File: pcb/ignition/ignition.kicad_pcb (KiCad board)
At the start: 4 copper layers, 100 x 100 mm, 142 parts, among them IC1 LTC4151, IC2 LTC4151, IC3 LTC4151, IC4 LTC4151, IC5 LTC4151, IC6 LTC4151, IC7 ADP3335, IC8 STM32F437VIT6, J1 PSU, J10 CH2, J11 CH4, J12 ARM, J13 UART1, J14 UART2, J15 CH1, J16 CH3, J17 CH5, J2 LED1, J3 PSU, J4 LED2, J5 5v In, J6 5v Out, J7 LED3, J8 LED4, J9 LED5, K1 16A SPST, K2 16A SPST, K3 16A SPST, K4 16A SPST, K5 16A SPST, K6 16A SPST, P1 SWD_TC, Q1 NFET, Q2 NFET, Q3 NFET, Q4 NFET, Q5 NFET, Q6 NFET, U1 MICROSD, X33 Hole, X34 Hole, X35 Hole, X36 Hole, Y1 26M

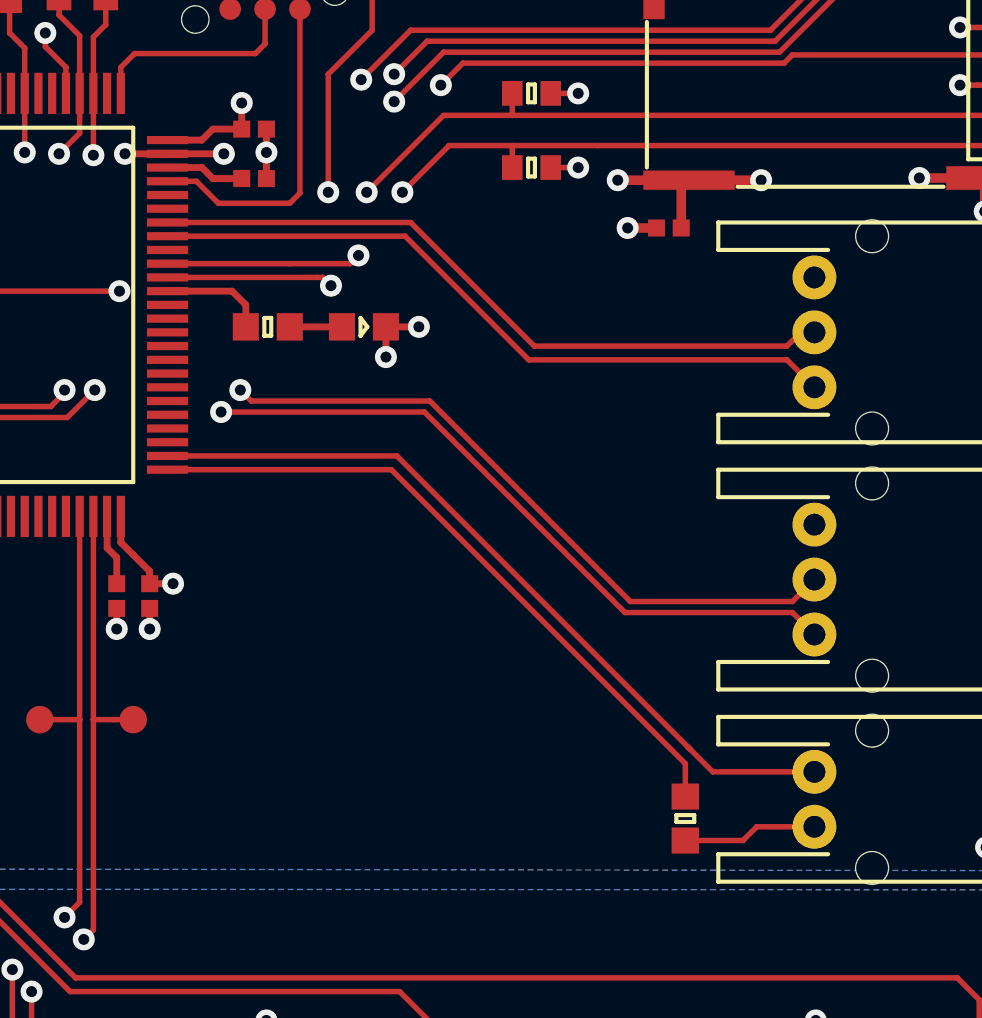
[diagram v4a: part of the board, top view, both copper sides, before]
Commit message: finalised schematic and pcb copper, adding silk
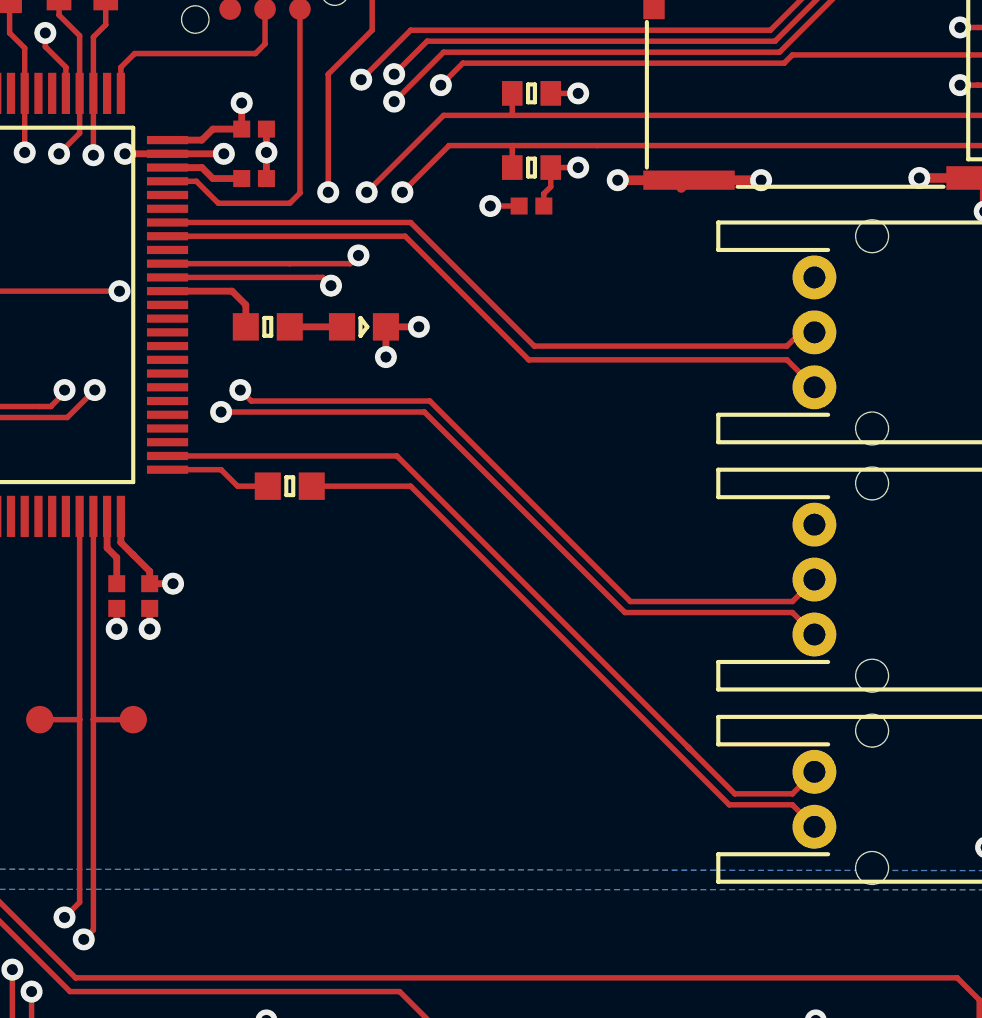
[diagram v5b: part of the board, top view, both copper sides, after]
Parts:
- moved R27 18.8 mm to (91.9, 45.6), turned to 180 degrees
- moved C19 5.06 mm to (100.7, 35.4), turned to 180 degrees
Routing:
- net /ARM_GRN: track 24.5 -> 3.90 mm
- net Net-(J12-Pad1): track 4.91 -> 23.4 mm
- net /ARM_RED: track 28.5 -> 29.1 mm
- net 3v3: track 227.3 -> 227.7 mm, vias 21 -> 20
- net GND: track 185.4 -> 185.0 mm, vias 84 -> 85
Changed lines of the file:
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@@
     (thickness 1.6)
     (drawings 4)
-    (tracks 1173)
+    (tracks 1177)
     (zones 0)
     (modules 142)
@@
   )
   (module agg:0402 (layer F.Cu)
-    (at 105.7 36.2)
-    (fp_text reference C19 (at -1.71 0 90) (layer F.Fab)
+    (at 100.7 35.4 180)
+    (fp_text reference C19 (at -1.71 0 270) (layer F.Fab)
       (effects (font (size 1 1) (thickness 0.15)))
     )
-    (fp_text value 100n (at 1.71 0 90) (layer F.Fab)
+    (fp_text value 100n (at 1.71 0 270) (layer F.Fab)
       (effects (font (size 1 1) (thickness 0.15)))
     )
@@
     (fp_line (start 0.5 -0.25) (end 0.5 0.25) (layer F.Fab) (width 0.01))
     (fp_line (start -0.5 -0.25) (end 0.5 -0.25) (layer F.Fab) (width 0.01))
-    (pad 2 smd rect (at 0.45 0) (size 0.62 0.62) (layers F.Cu F.Paste F.Mask)
+    (pad 2 smd rect (at 0.45 0 180) (size 0.62 0.62) (layers F.Cu F.Paste F.Mask)
       (net 2 GND))
-    (pad 1 smd rect (at -0.45 0) (size 0.62 0.62) (layers F.Cu F.Paste F.Mask)
+    (pad 1 smd rect (at -0.45 0 180) (size 0.62 0.62) (layers F.Cu F.Paste F.Mask)
       (net 15 3v3))
     (model ${KISYS3DMOD}/Resistors_SMD.3dshapes/R_0402.wrl
@@
   )
   (module agg:0603 (layer F.Cu)
-    (at 106.3 57.7 90)
-    (fp_text reference R27 (at -2.225 0 180) (layer F.Fab)
+    (at 91.9 45.6 180)
+    (fp_text reference R27 (at -2.225 0 270) (layer F.Fab)
       (effects (font (size 1 1) (thickness 0.15)))
     )
-    (fp_text value 100R (at 2.225 0 180) (layer F.Fab)
+    (fp_text value 100R (at 2.225 0 270) (layer F.Fab)
       (effects (font (size 1 1) (thickness 0.15)))
     )
@@
     (fp_line (start 0.8 -0.4) (end 0.8 0.4) (layer F.Fab) (width 0.01))
     (fp_line (start -0.8 -0.4) (end 0.8 -0.4) (layer F.Fab) (width 0.01))
-    (pad 2 smd rect (at 0.8 0 90) (size 0.95 1) (layers F.Cu F.Paste F.Mask)
+    (pad 2 smd rect (at 0.8 0 180) (size 0.95 1) (layers F.Cu F.Paste F.Mask)
       (net 76 /ARM_GRN))
-    (pad 1 smd rect (at -0.8 0 90) (size 0.95 1) (layers F.Cu F.Paste F.Mask)
+    (pad 1 smd rect (at -0.8 0 180) (size 0.95 1) (layers F.Cu F.Paste F.Mask)
       (net 122 "Net-(J12-Pad1)"))
     (model ${KISYS3DMOD}/Resistors_SMD.3dshapes/R_0603.wrl
@@
   (segment (start 117.2 35.16) (end 117.2 35.6) (width 0.35) (layer F.Cu) (net 2))
   (segment (start 106.15 34.745) (end 106.435 34.46) (width 0.35) (layer F.Cu) (net 2))
-  (segment (start 106.15 36.2) (end 106.15 34.745) (width 0.35) (layer F.Cu) (net 2))
+  (segment (start 100.25 35.4) (end 99.2 35.4) (width 0.2) (layer F.Cu) (net 2))
+  (via (at 99.2 35.4) (size 0.8) (drill 0.4) (layers F.Cu B.Cu) (net 2))
   (segment (start 43 95.8) (end 48.1 95.8) (width 0.35) (layer F.Cu) (net 3))
   (segment (start 48.1 95.8) (end 51 92.9) (width 0.35) (layer F.Cu) (net 3))
@@
   (via (at 116.3 28.9) (size 0.8) (drill 0.4) (layers F.Cu B.Cu) (net 15))
   (segment (start 116.95 28.9) (end 116.3 28.9) (width 0.2) (layer F.Cu) (net 15))
-  (via (at 104.2 36.2) (size 0.8) (drill 0.4) (layers F.Cu B.Cu) (net 15))
-  (segment (start 104.2 36.2) (end 105.25 36.2) (width 0.35) (layer F.Cu) (net 15))
   (segment (start 101.4 34) (end 102.4 34) (width 0.2) (layer F.Cu) (net 15))
   (via (at 102.4 34) (size 0.8) (drill 0.4) (layers F.Cu B.Cu) (net 15))
@@
   (segment (start 83.5 26.6) (end 83.5 25.6) (width 0.2) (layer F.Cu) (net 15))
   (via (at 83.5 25.6) (size 0.8) (drill 0.4) (layers F.Cu B.Cu) (net 15))
+  (segment (start 101.15 35.4) (end 101.15 34.95) (width 0.2) (layer F.Cu) (net 15))
+  (segment (start 101.15 34.95) (end 101.4 34.7) (width 0.2) (layer F.Cu) (net 15))
+  (segment (start 101.4 34.7) (end 101.4 34) (width 0.2) (layer F.Cu) (net 15))
   (segment (start 56.15 102) (end 56.25 102.1) (width 0.35) (layer F.Cu) (net 16))
   (segment (start 53.8 102) (end 56.15 102) (width 0.35) (layer F.Cu) (net 16))
@@
   (segment (start 36 55.8) (end 36.7 55.1) (width 0.2) (layer F.Cu) (net 74))
   (segment (start 36.7 55.1) (end 61.7 55.1) (width 0.2) (layer F.Cu) (net 74))
-  (segment (start 87.45 45) (end 95.6 45) (width 0.2) (layer F.Cu) (net 76))
-  (segment (start 106.3 55.7) (end 106.3 56.9) (width 0.2) (layer F.Cu) (net 76))
-  (segment (start 95.6 45) (end 106.3 55.7) (width 0.2) (layer F.Cu) (net 76))
+  (segment (start 91.1 45.6) (end 90 45.6) (width 0.2) (layer F.Cu) (net 76))
+  (segment (start 89.4 45) (end 87.45 45) (width 0.2) (layer F.Cu) (net 76))
+  (segment (start 90 45.6) (end 89.4 45) (width 0.2) (layer F.Cu) (net 76))
   (segment (start 87.45 44.5) (end 95.8 44.5) (width 0.2) (layer F.Cu) (net 77))
-  (segment (start 107.3 56) (end 106.4 55.1) (width 0.2) (layer F.Cu) (net 77))
   (segment (start 95.8 44.5) (end 106.4 55.1) (width 0.2) (layer F.Cu) (net 77))
-  (segment (start 111 56) (end 107.3 56) (width 0.2) (layer F.Cu) (net 77))
   (segment (start 106.4 55.1) (end 106.5 55.2) (width 0.2) (layer F.Cu) (net 77))
+  (segment (start 110.2 56.8) (end 111 56) (width 0.2) (layer F.Cu) (net 77))
+  (segment (start 106.4 55.1) (end 108.1 56.8) (width 0.2) (layer F.Cu) (net 77))
+  (segment (start 108.1 56.8) (end 110.2 56.8) (width 0.2) (layer F.Cu) (net 77))
   (segment (start 87.45 38.5) (end 89.8 38.5) (width 0.25) (layer F.Cu) (net 80))
   (segment (start 90.3 39) (end 90.3 39.8) (width 0.25) (layer F.Cu) (net 80))
@@
   (segment (start 114 109.3) (end 115 108.3) (width 0.35) (layer F.Cu) (net 121))
   (segment (start 114 111.5) (end 114 109.3) (width 0.35) (layer F.Cu) (net 121))
-  (segment (start 108.4 58.5) (end 108.9 58) (width 0.2) (layer F.Cu) (net 122))
-  (segment (start 106.3 58.5) (end 108.4 58.5) (width 0.2) (layer F.Cu) (net 122))
-  (segment (start 111 58) (end 108.9 58) (width 0.2) (layer F.Cu) (net 122))
+  (segment (start 111 58) (end 110.20001 57.20001) (width 0.2) (layer F.Cu) (net 122))
+  (segment (start 110.20001 57.20001) (end 107.90001 57.20001) (width 0.2) (layer F.Cu) (net 122))
+  (segment (start 96.3 45.6) (end 92.7 45.6) (width 0.2) (layer F.Cu) (net 122))
+  (segment (start 107.90001 57.20001) (end 96.3 45.6) (width 0.2) (layer F.Cu) (net 122))
   (segment (start 47 92.96) (end 54.5 92.96) (width 3) (layer B.Cu) (net 126))
   (segment (start 50 87.4) (end 50 86.1) (width 0.25) (layer B.Cu) (net 126))

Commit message: pcbs complete
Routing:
- net GND: vias 85 -> 112
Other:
- outline, holes or cut-outs redrawn
- board text added: "+"
- board text added: "-"
- board text added: "11/11/18"
- board text added: "24v"
- board text added: "5v"
- board text added: "5v In"
- board text added: "ARM"
- board text added: "AUX"
- board text added: "BANK"
- board text added: "CH1"
- board text added: "CH2"
- board text added: "CH3"
- board text added: "CH4"
- board text added: "CH5"
- board text added: "GND"
- board text added: "Hybrid Ignition Controller"
- board text added: "Ignition Board"
- board text added: "MAIN"
- board text added: "Matt Coates"
- board text added: "UART"

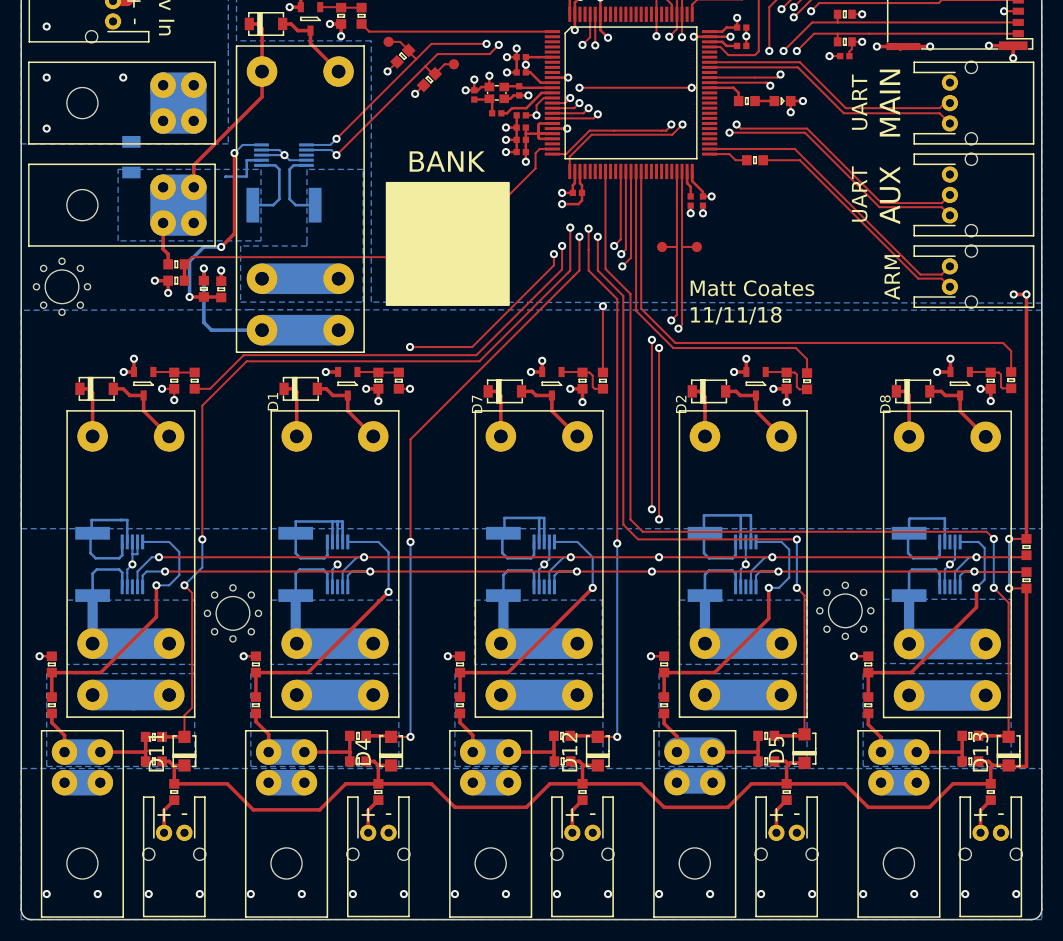
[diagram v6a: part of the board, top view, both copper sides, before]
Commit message: made changes to ignition as per review
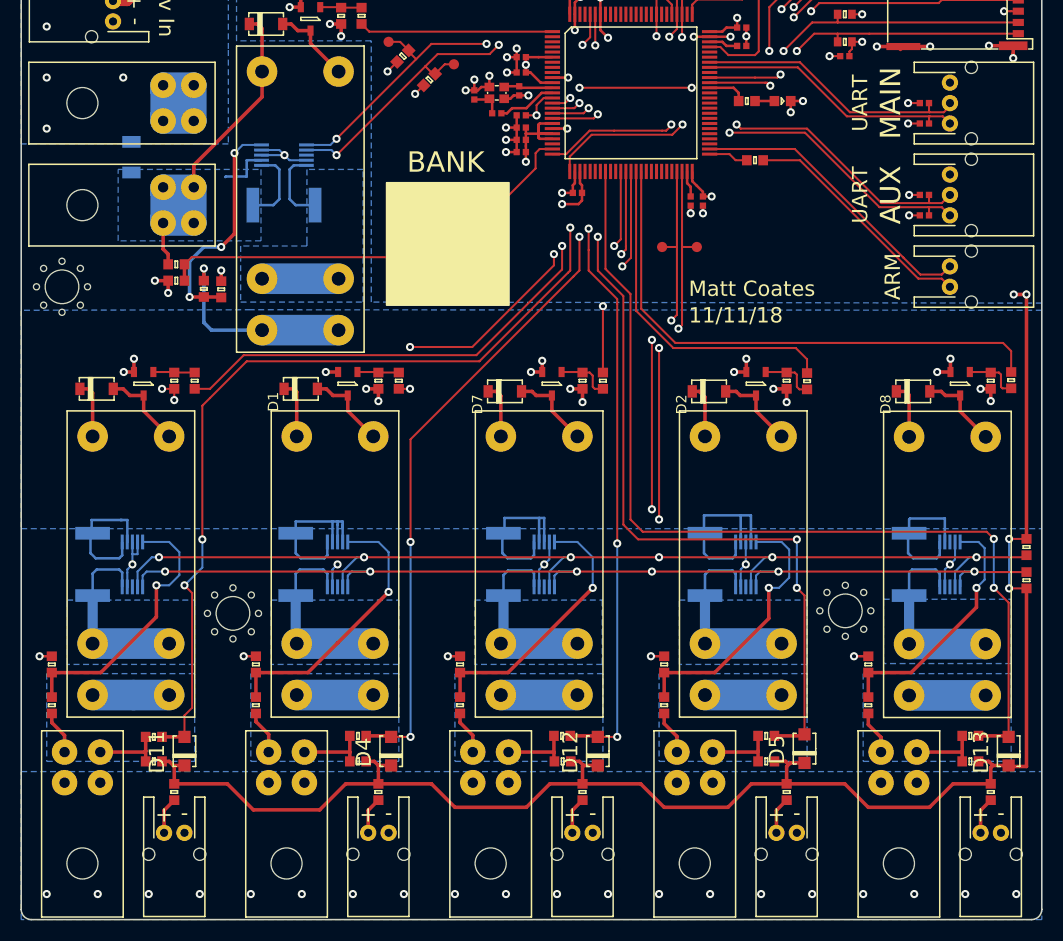
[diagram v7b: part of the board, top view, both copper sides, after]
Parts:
- added D14: ESD_DIODE, agg:0402, F.Cu at (108.5, 42.0)
- added D15: ESD_DIODE, agg:0402, F.Cu at (108.5, 40.0)
- added D16: ESD_DIODE, agg:0402, F.Cu at (108.5, 51.0)
- added D17: ESD_DIODE, agg:0402, F.Cu at (108.5, 49.0)
- C12: value 1µ -> 1u
- C17, C18: value 2µ2 -> 2u2
- C8: value 4µ7 -> 4u7
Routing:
- net GND: track 185.0 -> 171.9 mm, vias 112 -> 116
- net /CH5: track 22.3 -> 18.8 mm
- net /CH4: track 22.3 -> 18.8 mm
- net /CH3: track 22.3 -> 18.8 mm
- net /CH2: track 22.3 -> 18.8 mm
- net /CH1: track 22.2 -> 18.7 mm
- net /USART1_RX: track 25.6 -> 27.5 mm
- net /USART2_TX: track 43.9 -> 44.7 mm
- net /USART2_RX: track 43.5 -> 44.3 mm
- net /USART1_TX: track 25.8 -> 26.5 mm
